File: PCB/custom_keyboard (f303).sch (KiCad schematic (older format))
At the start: 368 parts, among them J1 Conn_01x04, J2 SM04B-SRSS-TB(LF)(SN), Q1 2N7002, SW1 SW_Push, U1 SRV05-4, U12 XC6206P332MR, U13 74LVC1G34, U14 STM32F303CBT6, X1 TestPoint_Small, X2 TestPoint_Small, Y2 8MHz

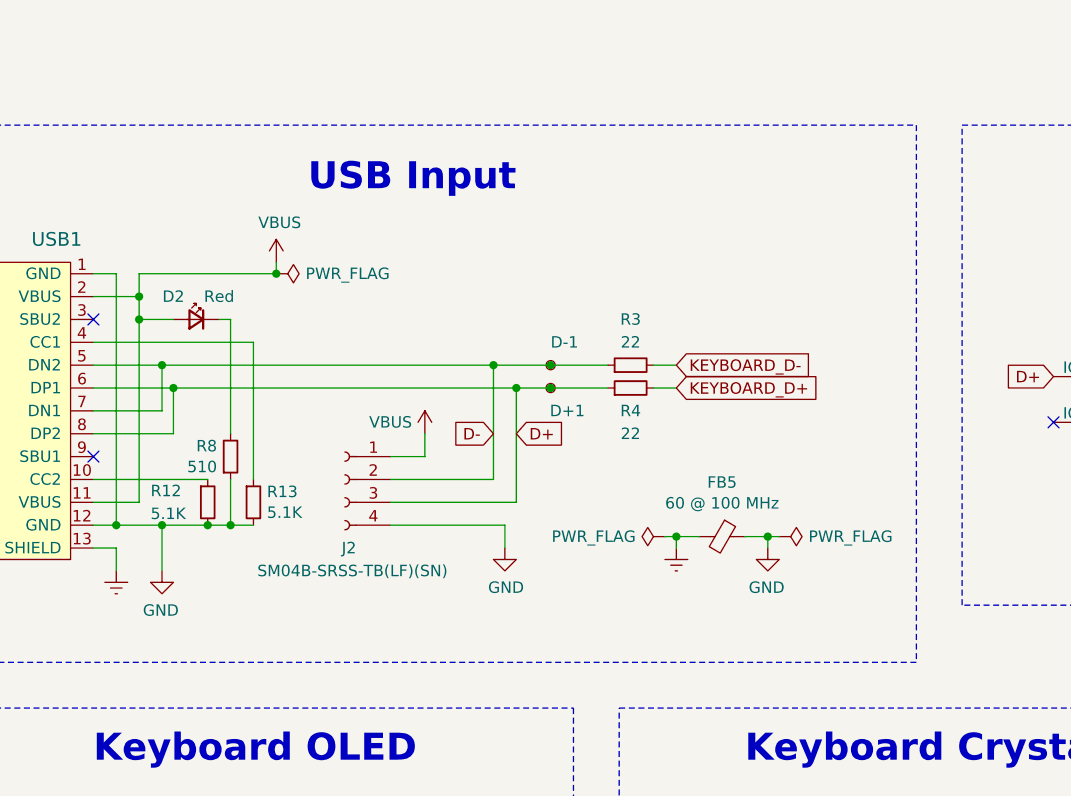
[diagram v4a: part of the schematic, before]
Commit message: Changed JST and button compoent
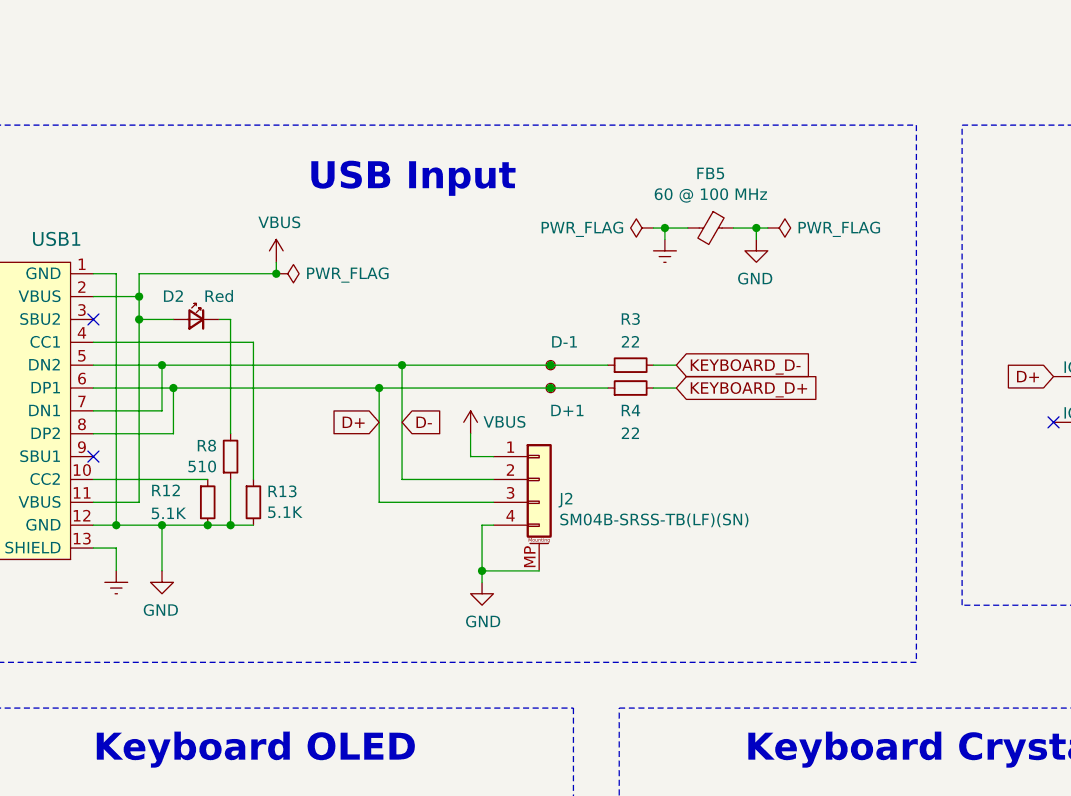
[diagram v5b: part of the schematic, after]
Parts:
- removed J2: SM04B-SRSS-TB(LF)(SN), random-keyboard-parts:JST-SR-4, symbol Connector:Conn_01x04_Female
- added J2: SM04B-SRSS-TB(LF)(SN), custom-footprints:JST-SR-4, symbol Connector_Generic_MountingPin:Conn_01x04_MountingPin
- SW1: footprint random-keyboard-parts:SKQG-1155865 -> custom-footprints:SKQG-1155865
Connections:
- net D+: now also J2.3 (Pin_3)
- net D-: now also J2.2 (Pin_2)
- net GND: now also J2.4 (Pin_4), J2.MP (MountPin)
- net VBUS: now also J2.1 (Pin_1)
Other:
- moved on the sheet: FB5
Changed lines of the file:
@@
 Text Notes 10600 12200 2    118  ~ 24
 USB Input
-Text GLabel 10500 13250 0    50   Input ~ 0
+Text GLabel 10100 13200 2    50   Input ~ 0
 D-
-Text GLabel 10600 13250 2    50   Input ~ 0
+Text GLabel 10000 13200 0    50   Input ~ 0
 D+
 Wire Wire Line
-	10500 12950 10750 12950
-Wire Wire Line
-	9050 12950 10500 12950
-Connection ~ 10500 12950
-Wire Wire Line
-	10600 13050 10750 13050
-Wire Wire Line
-	9100 13050 10600 13050
-Connection ~ 10600 13050
-Wire Wire Line
-	10200 13350 10200 13250
-Wire Wire Line
-	10050 13350 10200 13350
+	9100 13050 10000 13050
 $Comp
 L Device:Ferrite_Bead_Small FB5
 U 1 1 66EC0E90
-P 11500 13700
-F 0 "FB5" V 11263 13700 50  0000 C CNN
-F 1 "60 @ 100 MHz" V 11354 13700 50  0000 C CNN
-F 2 "Inductor_SMD:L_0805_2012Metric" V 11430 13700 50  0001 C CNN
-F 3 "~" H 11500 13700 50  0001 C CNN
-F 4 "C337883" H 11500 13700 50  0001 C CNN "LCSC Part"
-	1    11500 13700
+P 11450 12350
+F 0 "FB5" V 11213 12350 50  0000 C CNN
+F 1 "60 @ 100 MHz" V 11304 12350 50  0000 C CNN
+F 2 "Inductor_SMD:L_0805_2012Metric" V 11380 12350 50  0001 C CNN
+F 3 "~" H 11450 12350 50  0001 C CNN
+F 4 "C337883" H 11450 12350 50  0001 C CNN "LCSC Part"
+	1    11450 12350
 	0    1    1    0
 $EndComp
@@
 L power:GND #PWR0198
 U 1 1 66EC57B6
-P 11700 13750
-F 0 "#PWR0198" H 11700 13500 50  0001 C CNN
-F 1 "GND" H 11705 13577 50  0000 C CNN
-F 2 "" H 11700 13750 50  0001 C CNN
-F 3 "" H 11700 13750 50  0001 C CNN
-	1    11700 13750
+P 11650 12400
+F 0 "#PWR0198" H 11650 12150 50  0001 C CNN
+F 1 "GND" H 11655 12227 50  0000 C CNN
+F 2 "" H 11650 12400 50  0001 C CNN
+F 3 "" H 11650 12400 50  0001 C CNN
+	1    11650 12400
 	-1   0    0    -1
 $EndComp
@@
 L power:Earth #PWR0197
 U 1 1 66EC6036
-P 11300 13750
-F 0 "#PWR0197" H 11300 13500 50  0001 C CNN
-F 1 "Earth" H 11300 13600 50  0001 C CNN
-F 2 "" H 11300 13750 50  0001 C CNN
-F 3 "~" H 11300 13750 50  0001 C CNN
-	1    11300 13750
+P 11250 12400
+F 0 "#PWR0197" H 11250 12150 50  0001 C CNN
+F 1 "Earth" H 11250 12250 50  0001 C CNN
+F 2 "" H 11250 12400 50  0001 C CNN
+F 3 "~" H 11250 12400 50  0001 C CNN
+	1    11250 12400
 	1    0    0    -1
 $EndComp
@@
 L power:PWR_FLAG #FLG01
 U 1 1 66EC6E9C
-P 11250 13700
-F 0 "#FLG01" H 11250 13775 50  0001 C CNN
-F 1 "PWR_FLAG" V 11250 13827 50  0000 L CNN
-F 2 "" H 11250 13700 50  0001 C CNN
-F 3 "~" H 11250 13700 50  0001 C CNN
-	1    11250 13700
+P 11200 12350
+F 0 "#FLG01" H 11200 12425 50  0001 C CNN
+F 1 "PWR_FLAG" V 11200 12477 50  0000 L CNN
+F 2 "" H 11200 12350 50  0001 C CNN
+F 3 "~" H 11200 12350 50  0001 C CNN
+	1    11200 12350
 	0    -1   -1   0
 $EndComp
@@
 L power:PWR_FLAG #FLG02
 U 1 1 66EC7565
-P 11750 13700
-F 0 "#FLG02" H 11750 13775 50  0001 C CNN
-F 1 "PWR_FLAG" V 11750 13828 50  0000 L CNN
-F 2 "" H 11750 13700 50  0001 C CNN
-F 3 "~" H 11750 13700 50  0001 C CNN
-	1    11750 13700
+P 11700 12350
+F 0 "#FLG02" H 11700 12425 50  0001 C CNN
+F 1 "PWR_FLAG" V 11700 12478 50  0000 L CNN
+F 2 "" H 11700 12350 50  0001 C CNN
+F 3 "~" H 11700 12350 50  0001 C CNN
+	1    11700 12350
 	0    1    1    0
 $EndComp
 Wire Wire Line
-	11700 13700 11700 13750
+	11650 12350 11650 12400
 Wire Wire Line
-	11750 13700 11700 13700
+	11700 12350 11650 12350
 Wire Wire Line
-	11700 13700 11600 13700
-Connection ~ 11700 13700
+	11650 12350 11550 12350
+Connection ~ 11650 12350
 Wire Wire Line
-	11400 13700 11300 13700
+	11350 12350 11250 12350
 Wire Wire Line
-	11300 13750 11300 13700
-Connection ~ 11300 13700
+	11250 12400 11250 12350
+Connection ~ 11250 12350
 Wire Wire Line
-	11300 13700 11250 13700
+	11250 12350 11200 12350
 Wire Notes Line
 	12350 14250 7900 14250
 $Comp
-L Connector:Conn_01x04_Female J2
-U 1 1 665FCD92
-P 9850 13450
-F 0 "J2" H 9800 13150 50  0000 L CNN
-F 1 "SM04B-SRSS-TB(LF)(SN)" H 9400 13050 50  0000 L CNN
-F 2 "random-keyboard-parts:JST-SR-4" H 9850 13450 50  0001 C CNN
-F 3 "~" H 9850 13450 50  0001 C CNN
-F 4 "C160404" H 9850 13450 50  0001 C CNN "LCSC Part"
-	1    9850 13450
-	-1   0    0    -1
-$EndComp
-$Comp
 L power:GND #PWR0186
 U 1 1 6A8298AD
-P 10550 13750
-F 0 "#PWR0186" H 10550 13500 50  0001 C CNN
-F 1 "GND" H 10555 13577 50  0000 C CNN
-F 2 "" H 10550 13750 50  0001 C CNN
-F 3 "" H 10550 13750 50  0001 C CNN
-	1    10550 13750
+P 10450 13900
+F 0 "#PWR0186" H 10450 13650 50  0001 C CNN
+F 1 "GND" H 10455 13727 50  0000 C CNN
+F 2 "" H 10450 13900 50  0001 C CNN
+F 3 "" H 10450 13900 50  0001 C CNN
+	1    10450 13900
 	1    0    0    -1
 $EndComp
-Wire Wire Line
-	10050 13650 10550 13650
-Wire Wire Line
-	10550 13650 10550 13750
-Wire Wire Line
-	10500 12950 10500 13450
-Wire Wire Line
-	10500 13450 10050 13450
-Wire Wire Line
-	10600 13550 10600 13050
-Wire Wire Line
-	10050 13550 10600 13550
 $Comp
 L power:VBUS #PWR0184
@@
 L power:VBUS #PWR0185
 U 1 1 6D549A45
-P 10200 13250
-F 0 "#PWR0185" H 10200 13100 50  0001 C CNN
-F 1 "VBUS" H 10050 13300 50  0000 C CNN
-F 2 "" H 10200 13250 50  0001 C CNN
-F 3 "" H 10200 13250 50  0001 C CNN
-	1    10200 13250
-	1    0    0    -1
+P 10400 13250
+F 0 "#PWR0185" H 10400 13100 50  0001 C CNN
+F 1 "VBUS" H 10250 13300 50  0000 C CNN
+F 2 "" H 10400 13250 50  0001 C CNN
+F 3 "" H 10400 13250 50  0001 C CNN
+	1    10400 13250
+	-1   0    0    -1
 $EndComp
 $Comp
@@
 Wire Notes Line
 	7900 18450 7900 19700
-$Comp
-L Connector_Generic:Conn_01x04 J1
-U 1 1 AA803D2B
-P 9400 19150
-F 0 "J1" H 9318 19467 50  0000 C CNN
-F 1 "Conn_01x04" H 9318 19376 50  0000 C CNN
-F 2 "Connector_PinSocket_2.54mm:PinSocket_1x04_P2.54mm_Vertical" H 9400 19150 50  0001 C CNN
-F 3 "~" H 9400 19150 50  0001 C CNN
-F 4 "0" H 9400 19150 50  0001 C CNN "JLCPCB BOM"
-	1    9400 19150
-	1    0    0    -1
-$EndComp
 Wire Wire Line
 	9100 19350 9200 19350
@@
 F 0 "SW1" V 8546 17002 50  0000 R CNN
 F 1 "SW_Push" V 8455 17002 50  0000 R CNN
-F 2 "random-keyboard-parts:SKQG-1155865" H 8500 17250 50  0001 C CNN
+F 2 "custom-footprints:SKQG-1155865" H 8500 17250 50  0001 C CNN
 F 3 "~" H 8500 17250 50  0001 C CNN
 	1    8500 17050
@@
 	-1   0    0    -1
 $EndComp
+$Comp
+L Connector_Generic_MountingPin:Conn_01x04_MountingPin J2
+U 1 1 61F1E4EF
+P 10700 13450
+F 0 "J2" H 10788 13364 50  0000 L CNN
+F 1 "SM04B-SRSS-TB(LF)(SN)" H 10788 13273 50  0000 L CNN
+F 2 "custom-footprints:JST-SR-4" H 10700 13450 50  0001 C CNN
+F 3 "~" H 10700 13450 50  0001 C CNN
+	1    10700 13450
+	1    0    0    -1
+$EndComp
+$Comp
+L Connector_Generic:Conn_01x04 J1
+U 1 1 AA803D2B
+P 9400 19150
+F 0 "J1" H 9318 19467 50  0000 C CNN
+F 1 "Conn_01x04" H 9318 19376 50  0000 C CNN
+F 2 "Connector_PinSocket_2.54mm:PinSocket_1x04_P2.54mm_Vertical" H 9400 19150 50  0001 C CNN
+F 3 "~" H 9400 19150 50  0001 C CNN
+F 4 "0" H 9400 19150 50  0001 C CNN "JLCPCB BOM"
+	1    9400 19150
+	1    0    0    -1
+$EndComp
+Wire Wire Line
+	10500 13350 10400 13350
+Wire Wire Line
+	10400 13350 10400 13250
+Wire Wire Line
+	9050 12950 10100 12950
+Wire Wire Line
+	10000 13550 10000 13050
+Connection ~ 10000 13050
+Wire Wire Line
+	10000 13550 10500 13550
+Wire Wire Line
+	10000 13050 10750 13050
+Wire Wire Line
+	10500 13450 10100 13450
+Wire Wire Line
+	10100 13450 10100 12950
+Connection ~ 10100 12950
+Wire Wire Line
+	10100 12950 10750 12950
+Wire Wire Line
+	10500 13650 10450 13650
+Wire Wire Line
+	10450 13650 10450 13850
+Wire Wire Line
+	10700 13850 10450 13850
+Wire Wire Line
+	10450 13850 10450 13900
+Connection ~ 10450 13850
 $EndSCHEMATC

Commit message: Replaced footprints
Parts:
- removed C1: 100uF, Capacitor_SMD:C_1206_3216Metric, symbol Device:C_Small
- removed F1: 500mA, Fuse:Fuse_1206_3216Metric, symbol Device:Polyfuse_Small
- removed LED10, LED11, LED12, LED13, LED14, LED15, LED16, LED17, LED18, LED19, LED2, LED20, LED21, LED22, LED23, LED24, LED25, LED26, LED27, LED28, LED29, LED3, LED30, LED31, LED32, LED33, LED34, LED35, LED36, LED37, LED38, LED39, LED4, LED40, LED41, LED42, LED43, LED44, LED45, LED46, LED47, LED48, LED49, LED5, LED50, LED51, LED52, LED53, LED54, LED55, LED56, LED57, LED58, LED59, LED6, LED60, LED61, LED62, LED63, LED64, LED65, LED66, LED67, LED68, LED69, LED7, LED70, LED71, LED72, LED73, LED74, LED75, LED76, LED77, LED78, LED79, LED8, LED80, LED81, LED82, LED83, LED84, LED85, LED86, LED87, LED88, LED89, LED9, LED90: LED_ARGB, random-keyboard-parts:RGB-6028, symbol Device:LED_ARGB
- added LED10, LED11, LED12, LED13, LED14, LED15, LED16, LED17, LED18, LED19, LED2, LED20, LED21, LED22, LED23, LED24, LED25, LED26, LED27, LED28, LED29, LED3, LED30, LED31, LED32, LED33, LED34, LED35, LED36, LED37, LED38, LED39, LED4, LED40, LED41, LED42, LED43, LED44, LED45, LED46, LED47, LED48, LED49, LED5, LED50, LED51, LED52, LED53, LED54, LED55, LED56, LED57, LED58, LED59, LED6, LED60, LED61, LED62, LED63, LED64, LED65, LED66, LED67, LED68, LED69, LED7, LED70, LED71, LED72, LED73, LED74, LED75, LED76, LED77, LED78, LED79, LED8, LED80, LED81, LED82, LED83, LED84, LED85, LED86, LED87, LED88, LED89, LED9, LED90: LED_ABGR, custom-footprints:MHT151RGBCT_with_outline, symbol Device:LED_ABGR
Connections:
- net 1CA1: now also LED1.4 (RK), LED2.4 (RK), LED3.4 (RK), LED4.4 (RK), LED5.4 (RK), LED6.4 (RK), LED7.4 (RK), LED8.4 (RK), LED9.1 (A); no longer LED1.2 (BK)
- net 1CA2: now also LED10.1 (A), LED2.3 (GK), LED3.3 (GK), LED4.3 (GK), LED5.3 (GK), LED6.3 (GK), LED7.3 (GK), LED8.3 (GK)
- net 1CA3: now also LED11.1 (A), LED2.1 (A), LED3.2 (BK), LED4.2 (BK), LED5.2 (BK), LED6.2 (BK), LED7.2 (BK), LED8.2 (BK)
- net 1CA4: now also LED1.2 (BK), LED12.1 (A), LED2.2 (BK), LED3.1 (A); no longer LED1.4 (RK)
- net 1CA5: now also LED13.1 (A), LED4.1 (A)
- net 1CA6: now also LED14.1 (A), LED15.2 (BK), LED16.2 (BK), LED5.1 (A)
- net 1CA7: now also LED10.2 (BK), LED11.2 (BK), LED12.2 (BK), LED13.2 (BK), LED14.2 (BK), LED15.1 (A), LED16.3 (GK), LED6.1 (A), LED9.2 (BK)
- net 1CA8: now also LED10.3 (GK), LED11.3 (GK), LED12.3 (GK), LED13.3 (GK), LED14.3 (GK), LED15.3 (GK), LED16.1 (A), LED7.1 (A), LED9.3 (GK)
- net 1CA9: now also LED10.4 (RK), LED11.4 (RK), LED12.4 (RK), LED13.4 (RK), LED14.4 (RK), LED15.4 (RK), LED16.4 (RK), LED8.1 (A), LED9.4 (RK)
- net 1CB1: now also LED17.4 (RK), LED18.4 (RK), LED19.4 (RK), LED20.4 (RK), LED21.4 (RK), LED22.4 (RK), LED23.4 (RK), LED24.4 (RK), LED32.1 (A)
- net 1CB2: now also LED17.3 (GK), LED18.3 (GK), LED19.3 (GK), LED20.3 (GK), LED21.3 (GK), LED22.3 (GK), LED23.3 (GK), LED24.1 (A), LED31.1 (A)
- net 1CB3: now also LED17.2 (BK), LED18.2 (BK), LED19.2 (BK), LED20.2 (BK), LED21.2 (BK), LED22.2 (BK), LED23.1 (A), LED24.3 (GK), LED30.1 (A)
- net 1CB4: now also LED22.1 (A), LED23.2 (BK), LED24.2 (BK), LED29.1 (A)
- net 1CB5: now also LED21.1 (A), LED28.1 (A)
- net 1CB6: now also LED20.1 (A), LED25.2 (BK), LED26.2 (BK), LED27.1 (A)
- net 1CB7: now also LED19.1 (A), LED25.3 (GK), LED26.1 (A), LED27.2 (BK), LED28.2 (BK), LED29.2 (BK), LED30.2 (BK), LED31.2 (BK), LED32.2 (BK)
- net 1CB8: now also LED18.1 (A), LED25.1 (A), LED26.3 (GK), LED27.3 (GK), LED28.3 (GK), LED29.3 (GK), LED30.3 (GK), LED31.3 (GK), LED32.3 (GK)
- net 1CB9: now also LED17.1 (A), LED25.4 (RK), LED26.4 (RK), LED27.4 (RK), LED28.4 (RK), LED29.4 (RK), LED30.4 (RK), LED31.4 (RK), LED32.4 (RK)
- net 2CA1: now also LED33.4 (RK), LED34.4 (RK), LED35.4 (RK), LED36.4 (RK), LED37.4 (RK), LED38.4 (RK), LED39.4 (RK), LED40.4 (RK), LED41.1 (A)
- net 2CA2: now also LED33.1 (A), LED34.3 (GK), LED35.3 (GK), LED36.3 (GK), LED37.3 (GK), LED38.3 (GK), LED39.3 (GK), LED40.3 (GK), LED42.1 (A)
- net 2CA3: now also LED33.3 (GK), LED34.1 (A), LED35.2 (BK), LED36.2 (BK), LED37.2 (BK), LED38.2 (BK), LED39.2 (BK), LED40.2 (BK), LED43.1 (A)
- net 2CA4: now also LED33.2 (BK), LED34.2 (BK), LED35.1 (A), LED44.1 (A)
- net 2CA5: now also LED36.1 (A), LED45.1 (A)
- net 2CA6: now also LED37.1 (A), LED46.1 (A), LED47.2 (BK), LED48.2 (BK)
- net 2CA7: now also LED38.1 (A), LED41.2 (BK), LED42.2 (BK), LED43.2 (BK), LED44.2 (BK), LED45.2 (BK), LED46.2 (BK), LED47.1 (A), LED48.3 (GK)
- net 2CA8: now also LED39.1 (A), LED41.3 (GK), LED42.3 (GK), LED43.3 (GK), LED44.3 (GK), LED45.3 (GK), LED46.3 (GK), LED47.3 (GK), LED48.1 (A)
- net 2CA9: now also LED40.1 (A), LED41.4 (RK), LED42.4 (RK), LED43.4 (RK), LED44.4 (RK), LED45.4 (RK), LED46.4 (RK), LED47.4 (RK), LED48.4 (RK)
- net 2CB1: now also LED49.4 (RK), LED50.4 (RK), LED51.4 (RK), LED52.4 (RK), LED53.4 (RK), LED54.4 (RK), LED55.4 (RK), LED56.4 (RK), LED64.1 (A)
- net 2CB2: now also LED49.3 (GK), LED50.3 (GK), LED51.3 (GK), LED52.3 (GK), LED53.3 (GK), LED54.3 (GK), LED55.3 (GK), LED56.1 (A), LED63.1 (A)
- net 2CB3: now also LED49.2 (BK), LED50.2 (BK), LED51.2 (BK), LED52.2 (BK), LED53.2 (BK), LED54.2 (BK), LED55.1 (A), LED56.3 (GK), LED62.1 (A)
- net 2CB4: now also LED54.1 (A), LED55.2 (BK), LED56.2 (BK), LED61.1 (A)
- net 2CB5: now also LED53.1 (A), LED60.1 (A)
- net 2CB6: now also LED52.1 (A), LED57.2 (BK), LED58.2 (BK), LED59.1 (A)
- net 2CB7: now also LED51.1 (A), LED57.3 (GK), LED58.1 (A), LED59.2 (BK), LED60.2 (BK), LED61.2 (BK), LED62.2 (BK), LED63.2 (BK), LED64.2 (BK)
- net 2CB8: now also LED50.1 (A), LED57.1 (A), LED58.3 (GK), LED59.3 (GK), LED60.3 (GK), LED61.3 (GK), LED62.3 (GK), LED63.3 (GK), LED64.3 (GK)
- net 2CB9: now also LED49.1 (A), LED57.4 (RK), LED58.4 (RK), LED59.4 (RK), LED60.4 (RK), LED61.4 (RK), LED62.4 (RK), LED63.4 (RK), LED64.4 (RK)
- net 3CA1: now also LED65.4 (RK), LED66.4 (RK), LED67.4 (RK), LED68.4 (RK), LED69.4 (RK), LED70.4 (RK), LED71.4 (RK), LED72.4 (RK), LED73.1 (A)
- net 3CA2: now also LED65.1 (A), LED66.3 (GK), LED67.3 (GK), LED68.3 (GK), LED69.3 (GK), LED70.3 (GK), LED71.3 (GK), LED72.3 (GK), LED74.1 (A)
- net 3CA3: now also LED65.3 (GK), LED66.1 (A), LED67.2 (BK), LED68.2 (BK), LED69.2 (BK), LED70.2 (BK), LED71.2 (BK), LED72.2 (BK), LED75.1 (A)
- net 3CA4: now also LED65.2 (BK), LED66.2 (BK), LED67.1 (A), LED76.1 (A)
- net 3CA5: now also LED68.1 (A), LED77.1 (A)
- net 3CA6: now also LED69.1 (A), LED78.1 (A), LED79.2 (BK), LED80.2 (BK)
- net 3CA7: now also LED70.1 (A), LED73.2 (BK), LED74.2 (BK), LED75.2 (BK), LED76.2 (BK), LED77.2 (BK), LED78.2 (BK), LED79.1 (A), LED80.3 (GK)
- net 3CA8: now also LED71.1 (A), LED73.3 (GK), LED74.3 (GK), LED75.3 (GK), LED76.3 (GK), LED77.3 (GK), LED78.3 (GK), LED79.3 (GK), LED80.1 (A)
- net 3CA9: now also LED72.1 (A), LED73.4 (RK), LED74.4 (RK), LED75.4 (RK), LED76.4 (RK), LED77.4 (RK), LED78.4 (RK), LED79.4 (RK), LED80.4 (RK)
- net 3CB1: now also LED81.4 (RK), LED82.4 (RK), LED83.4 (RK), LED84.4 (RK), LED85.4 (RK), LED86.4 (RK), LED87.4 (RK), LED88.4 (RK)
- net 3CB2: now also LED81.3 (GK), LED82.3 (GK), LED83.3 (GK), LED84.3 (GK), LED85.3 (GK), LED86.3 (GK), LED87.3 (GK), LED88.1 (A)
- net 3CB3: now also LED81.2 (BK), LED82.2 (BK), LED83.2 (BK), LED84.2 (BK), LED85.2 (BK), LED86.2 (BK), LED87.1 (A), LED88.3 (GK)
- net 3CB4: now also LED86.1 (A), LED87.2 (BK), LED88.2 (BK)
- net 3CB5: now also LED85.1 (A)
- net 3CB6: now also LED84.1 (A), LED89.2 (BK), LED90.2 (BK)
- net 3CB7: now also LED83.1 (A), LED89.3 (GK), LED90.1 (A)
- net 3CB8: now also LED82.1 (A), LED89.1 (A), LED90.3 (GK)
- net 3CB9: now also LED81.1 (A), LED89.4 (RK), LED90.4 (RK)
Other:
- note removed: "LED Fuse"
- moved on the sheet: LED1

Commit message: Routed LEDs on 1CB
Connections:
- net 1CB1: now also LED25.1 (A); no longer LED32.1 (A)
- net 1CB2: now also LED17.1 (A), LED24.3 (GK), LED26.1 (A); no longer LED17.3 (GK), LED24.1 (A), LED31.1 (A)
- net 1CB3: now also LED17.3 (GK), LED18.1 (A), LED23.2 (BK), LED24.2 (BK), LED27.1 (A); no longer LED17.2 (BK), LED18.2 (BK), LED23.1 (A), LED24.3 (GK), LED30.1 (A)
- net 1CB4: now also LED17.2 (BK), LED18.2 (BK), LED19.1 (A), LED28.1 (A); no longer LED22.1 (A), LED23.2 (BK), LED24.2 (BK), LED29.1 (A)
- net 1CB5: now also LED20.1 (A), LED29.1 (A); no longer LED21.1 (A), LED28.1 (A)
- net 1CB6: now also LED21.1 (A), LED30.1 (A), LED31.2 (BK), LED32.2 (BK); no longer LED20.1 (A), LED25.2 (BK), LED26.2 (BK), LED27.1 (A)
- net 1CB7: now also LED22.1 (A), LED25.2 (BK), LED26.2 (BK), LED31.1 (A), LED32.3 (GK); no longer LED19.1 (A), LED25.3 (GK), LED26.1 (A), LED31.2 (BK), LED32.2 (BK)
- net 1CB8: now also LED23.1 (A), LED25.3 (GK), LED32.1 (A); no longer LED18.1 (A), LED25.1 (A), LED32.3 (GK)
- net 1CB9: now also LED24.1 (A); no longer LED17.1 (A)

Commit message: Connected I1 to MCU
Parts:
- removed LED89, LED90: LED_ABGR, custom-footprints:MHT151RGBCT_with_outline, symbol Device:LED_ABGR
- added LED95, LED96: LED_ABGR, custom-footprints:MHT151RGBCT_with_outline, symbol Device:LED_ABGR
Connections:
- net 2CB1: now also LED57.1 (A); no longer LED64.1 (A)
- net 2CB2: now also LED49.1 (A), LED56.3 (GK), LED58.1 (A); no longer LED49.3 (GK), LED56.1 (A), LED63.1 (A)
- net 2CB3: now also LED49.3 (GK), LED50.1 (A), LED55.2 (BK), LED56.2 (BK), LED59.1 (A); no longer LED49.2 (BK), LED50.2 (BK), LED55.1 (A), LED56.3 (GK), LED62.1 (A)
- net 2CB4: now also LED49.2 (BK), LED50.2 (BK), LED51.1 (A), LED60.1 (A); no longer LED54.1 (A), LED55.2 (BK), LED56.2 (BK), LED61.1 (A)
- net 2CB5: now also LED52.1 (A), LED61.1 (A); no longer LED53.1 (A), LED60.1 (A)
- net 2CB6: now also LED53.1 (A), LED62.1 (A), LED63.2 (BK), LED64.2 (BK); no longer LED52.1 (A), LED57.2 (BK), LED58.2 (BK), LED59.1 (A)
- net 2CB7: now also LED54.1 (A), LED57.2 (BK), LED58.2 (BK), LED63.1 (A), LED64.3 (GK); no longer LED51.1 (A), LED57.3 (GK), LED58.1 (A), LED63.2 (BK), LED64.2 (BK)
- net 2CB8: now also LED55.1 (A), LED57.3 (GK), LED64.1 (A); no longer LED50.1 (A), LED57.1 (A), LED64.3 (GK)
- net 2CB9: now also LED56.1 (A); no longer LED49.1 (A)
- net 3CB2: now also LED81.1 (A), LED88.3 (GK); no longer LED81.3 (GK), LED88.1 (A)
- net 3CB3: now also LED81.3 (GK), LED82.1 (A), LED87.2 (BK), LED88.2 (BK); no longer LED81.2 (BK), LED82.2 (BK), LED87.1 (A), LED88.3 (GK)
- net 3CB4: now also LED81.2 (BK), LED82.2 (BK), LED83.1 (A); no longer LED86.1 (A), LED87.2 (BK), LED88.2 (BK)
- net 3CB5: now also LED84.1 (A); no longer LED85.1 (A)
- net 3CB6: now also LED85.1 (A), LED95.2 (BK), LED96.2 (BK); no longer LED84.1 (A)
- net 3CB7: now also LED86.1 (A), LED95.1 (A), LED96.3 (GK); no longer LED83.1 (A)
- net 3CB8: now also LED87.1 (A), LED95.3 (GK), LED96.1 (A); no longer LED82.1 (A)
- net 3CB9: now also LED88.1 (A), LED95.4 (RK), LED96.4 (RK); no longer LED81.1 (A)
